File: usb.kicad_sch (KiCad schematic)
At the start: 9 parts, among them J1 GSB1C411111DS1HR, U1 TPS7B8133DRVR

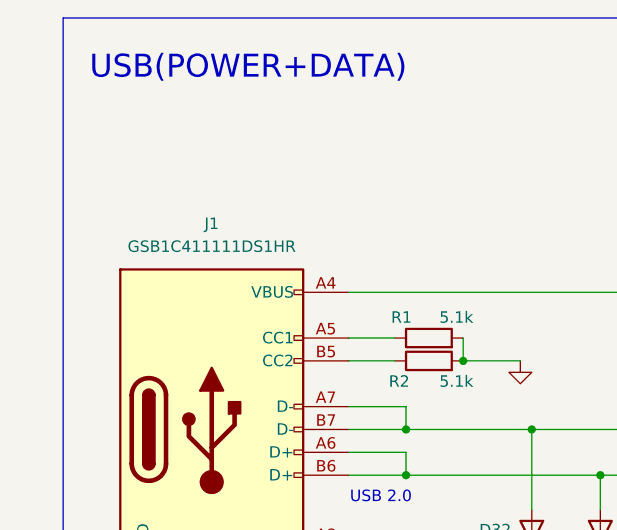
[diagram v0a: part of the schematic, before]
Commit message: rewired most lines, changed sizes to make easier to solder
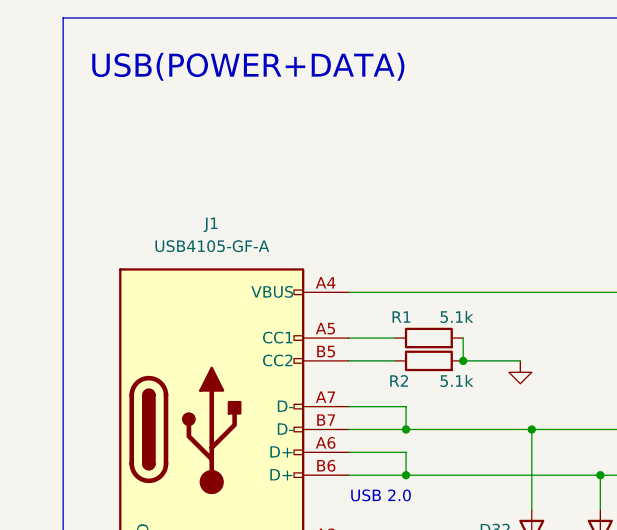
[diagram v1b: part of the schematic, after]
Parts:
- J1: value GSB1C411111DS1HR -> USB4105-GF-A; footprint usb_personal:AMPHENOL_GSB1C411111DS1HR -> Connector_USB:USB_C_Receptacle_GCT_USB4105-xx-A_16P_TopMnt_Horizontal
- R1, R2: footprint Resistor_SMD:R_0402_1005Metric -> Resistor_SMD:R_0603_1608Metric
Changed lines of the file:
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@@
 			)
 		)
-		(property "Footprint" "Resistor_SMD:R_0402_1005Metric"
+		(property "Footprint" "Resistor_SMD:R_0603_1608Metric"
 			(at 119.38 90.678 90)
 			(effects
@@
 			)
 		)
-		(property "Footprint" "Resistor_SMD:R_0402_1005Metric"
+		(property "Footprint" "Resistor_SMD:R_0603_1608Metric"
 			(at 119.38 88.138 90)
 			(effects
@@
 			)
 		)
-		(property "Value" "GSB1C411111DS1HR"
+		(property "Value" "USB4105-GF-A"
 			(at 95.25 76.2 0)
 			(effects
@@
 			)
 		)
-		(property "Footprint" "usb_personal:AMPHENOL_GSB1C411111DS1HR"
+		(property "Footprint" "Connector_USB:USB_C_Receptacle_GCT_USB4105-xx-A_16P_TopMnt_Horizontal"
 			(at 99.06 96.52 0)
 			(effects

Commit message: board completed
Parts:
- D31: value 82306050029 -> PESD5V0S1BA,115; footprint Diode_SMD:D_0603_1608Metric -> Diode_SMD:D_SOD-323F
- D32, D33: value 82306050029 -> STS321050B100; footprint Diode_SMD:D_0603_1608Metric -> Diode_SMD:D_SOD-323F
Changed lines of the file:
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@@
 			)
 		)
-		(property "Value" "82306050029"
-			(at 115.316 110.49 90)
-			(effects
-				(font
-					(size 1.27 1.27)
-				)
-				(justify right)
-			)
-		)
-		(property "Footprint" "Diode_SMD:D_0603_1608Metric"
+		(property "Value" "STS321050B100"
+			(at 113.792 110.49 90)
+			(effects
+				(font
+					(size 1.27 1.27)
+				)
+				(justify right)
+			)
+		)
+		(property "Footprint" "Diode_SMD:D_SOD-323F"
 			(at 130.81 109.22 0)
 			(effects
@@
 			)
 		)
-		(property "Value" "82306050029"
+		(property "Value" "STS321050B100"
 			(at 140.97 110.4899 90)
 			(effects
@@
 			)
 		)
-		(property "Footprint" "Diode_SMD:D_0603_1608Metric"
+		(property "Footprint" "Diode_SMD:D_SOD-323F"
 			(at 138.43 109.22 0)
 			(effects
@@
 			)
 		)
-		(property "Value" "82306050029"
+		(property "Value" "PESD5V0S1BA,115"
 			(at 146.05 87.6299 90)
 			(effects
@@
 			)
 		)
-		(property "Footprint" "Diode_SMD:D_0603_1608Metric"
+		(property "Footprint" "Diode_SMD:D_SOD-323F"
 			(at 143.51 86.36 0)
 			(effects
